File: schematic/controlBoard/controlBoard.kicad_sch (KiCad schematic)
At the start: 42 parts, among them J1 Conn_01x10_Pin, J2 USB_C_Receptacle_USB2.0_14P, T1 BC847, T2 BC847, U1 ESP-12E, U2 LM1117DT-3.3, U3 CH340G, U4 DS3231M, Y1 12MHz

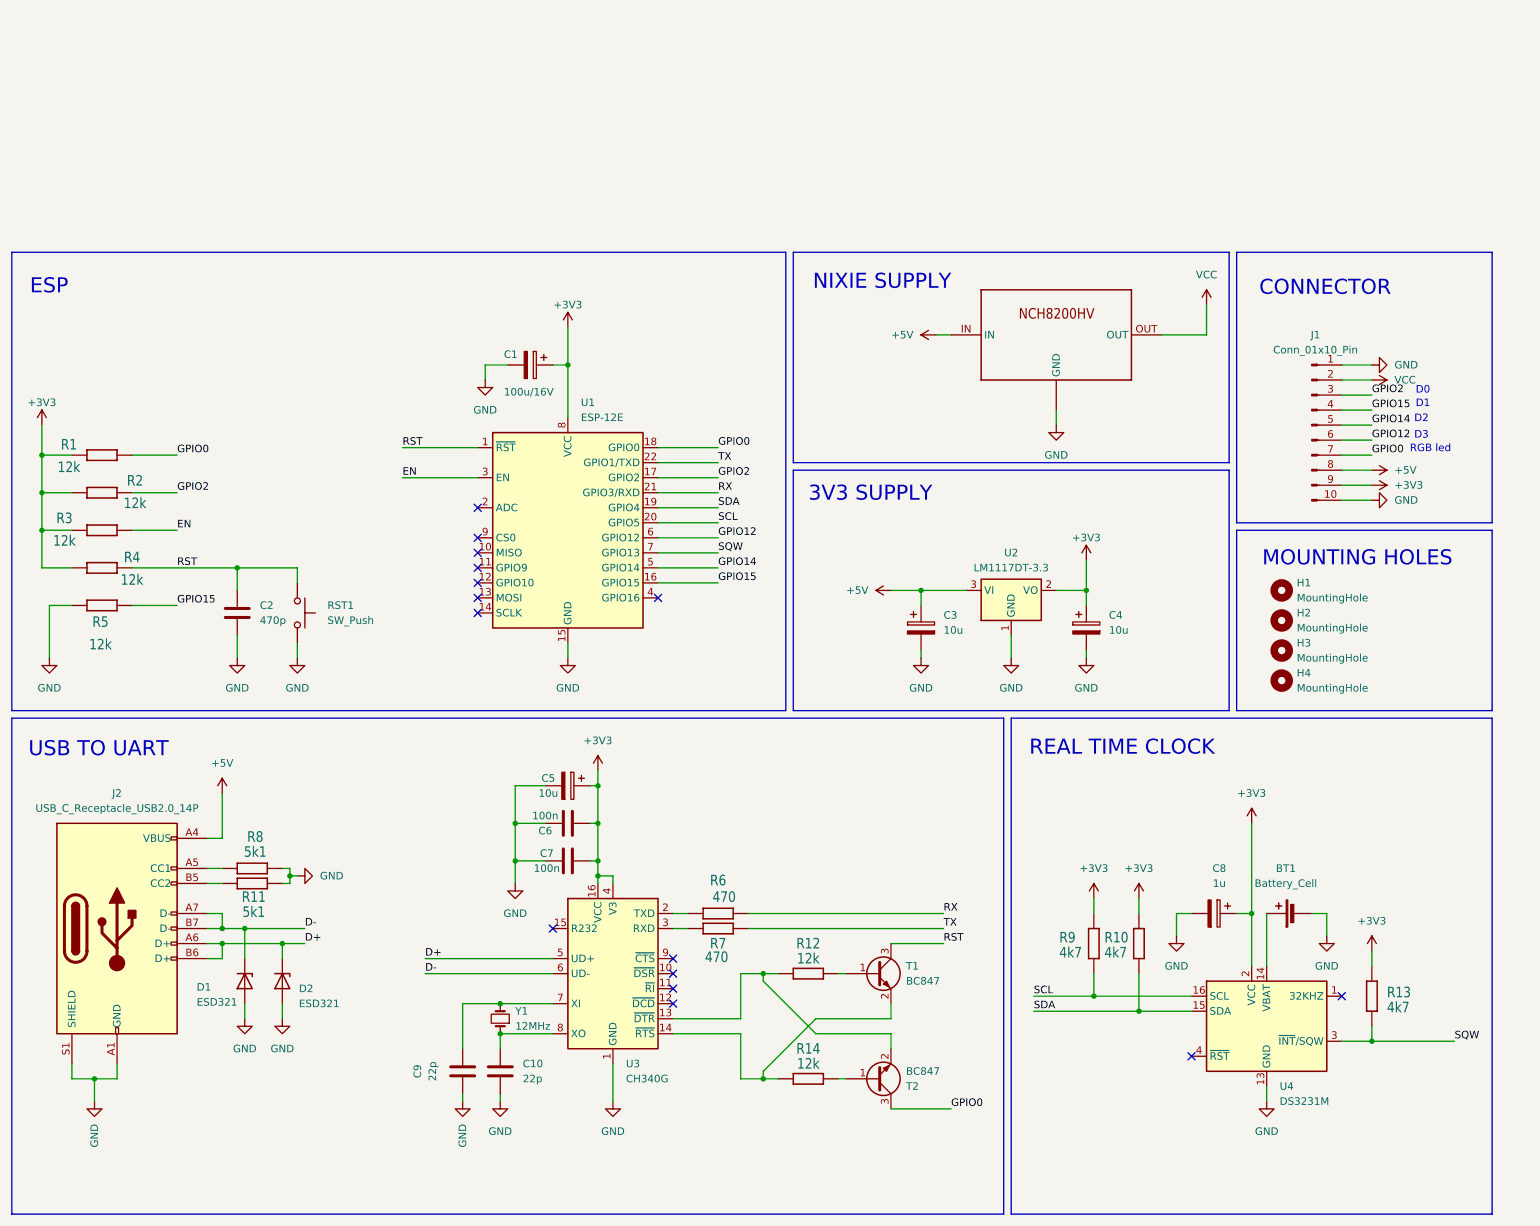
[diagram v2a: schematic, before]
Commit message: Use ESP32 instead of ESP8266
- Re-route PCB to support ESP32
- Fill top plane with +3v3
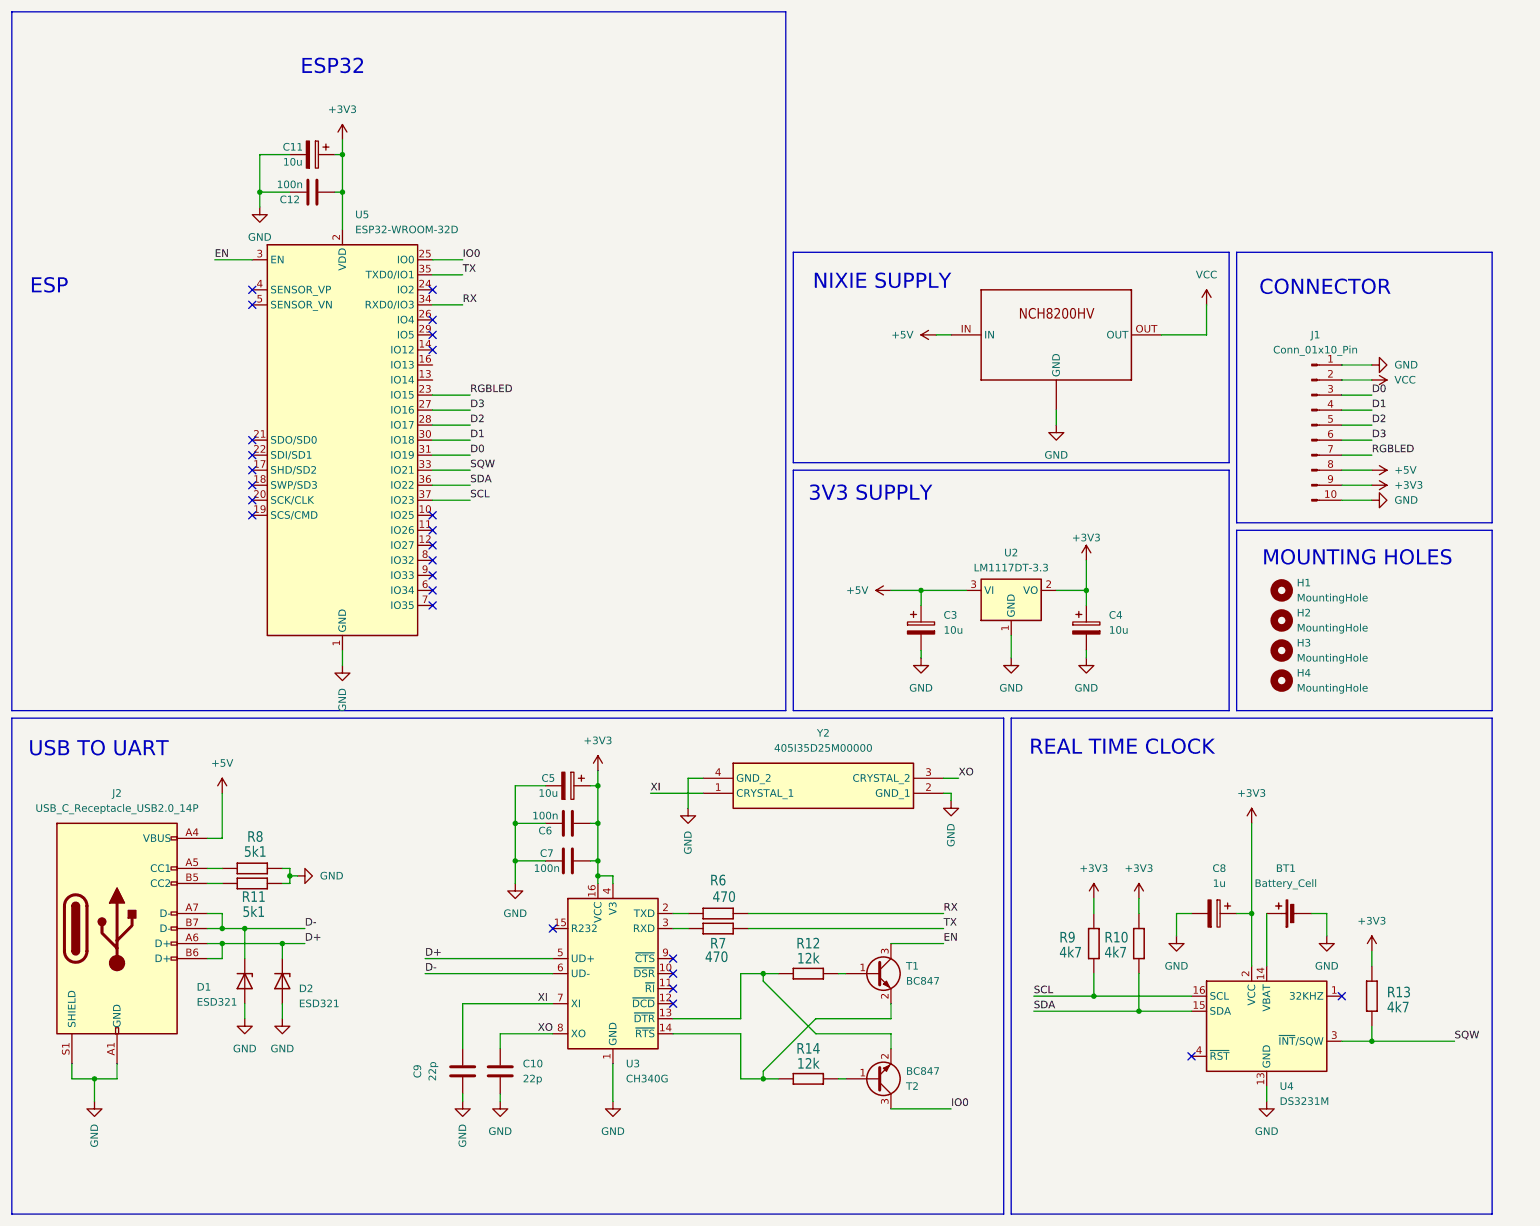
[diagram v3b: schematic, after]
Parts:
- removed C1: 100u/16V, Capacitor_Tantalum_SMD:CP_EIA-7343-31_Kemet-D, symbol Device:C_Polarized
- removed C2: 470p, Capacitor_SMD:C_0603_1608Metric, symbol Device:C
- removed R1, R2, R3, R4, R5: 12k, Resistor_SMD:R_0603_1608Metric, symbol controlBoard-eagle-import:R-EU_R0603
- removed RST1: SW_Push, Button_Switch_THT:SW_Tactile_SPST_Angled_PTS645Vx31-2LFS, symbol Switch:SW_Push
- removed U1: ESP-12E, RF_Module:ESP-12E, symbol RF_Module:ESP-12E
- removed Y1: 12MHz, controlBoard:CRYSTAL-SMD-5X3.2-4PAD, symbol Device:Crystal_Small
- added C11: 10u, Capacitor_Tantalum_SMD:CP_EIA-3216-10_Kemet-I, symbol Device:C_Polarized
- added C12: 100n, Capacitor_SMD:C_0603_1608Metric, symbol Device:C
- added U5: ESP32-WROOM-32D, RF_Module:ESP32-WROOM-32D-no-keepout, symbol RF_Module:ESP32-WROOM-32D
- added Y2: 405I35D25M00000, 405I35D25M00000, symbol cristal:405I35D25M00000
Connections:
- net RST is gone; now on net EN: T1.3 (C)
- net +3V3: now also C11.1, C12.1, U5.2 (VDD)
- net EN: now also U5.3 (EN)
- net GND: now also C11.2, C12.2, U5.1 (GND), U5.15 (GND), U5.38 (GND), U5.39 (GND), Y2.2 (GND_1), Y2.4 (GND_2)
- net RX: now also U5.34 (RXD0/IO3)
- net SCL: now also U5.37 (IO23)
- net SDA: now also U5.36 (IO22)
- net SQW: now also U5.33 (IO21)
- net TX: now also U5.35 (TXD0/IO1)
- net XI: now reaches C9.1, U3.7 (XI)
- net XI: now also Y2.1 (CRYSTAL_1)
- net XO: now reaches C10.1, U3.8 (XO)
- net XO: now also Y2.3 (CRYSTAL_2)
- net GPIO0 renamed IO0
- net IO0: now also U5.25 (IO0); no longer J1.7 (Pin_7)
- net GPIO12 renamed D3
- net D3: now also U5.27 (IO16)
- net GPIO14 renamed D2
- net D2: now also U5.28 (IO17)
- net GPIO15 renamed D1
- net D1: now also U5.30 (IO18)
- net GPIO2 renamed D0
- net D0: now also U5.31 (IO19)
- new net RGBLED: J1.7 (Pin_7), U5.23 (IO15)
- no-connect marks 15 -> 26
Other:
- note added: "ESP32"
- note removed: "D0"
- note removed: "D1"
- note removed: "D2"
- note removed: "D3"
- note removed: "RGB led"
